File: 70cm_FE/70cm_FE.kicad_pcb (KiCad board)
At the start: 2 copper layers, 50 x 70 mm, 181 parts, among them J2 U.FL, J3 U.FL, J4 U.FL, Q1 2SC3356, Q2 2SC3356, Q3 2SC3356, Q4 2SC3356, U1 HT7533-1, U2 74HC14, U3 74HC14, U4 LM393, U5 M68710L

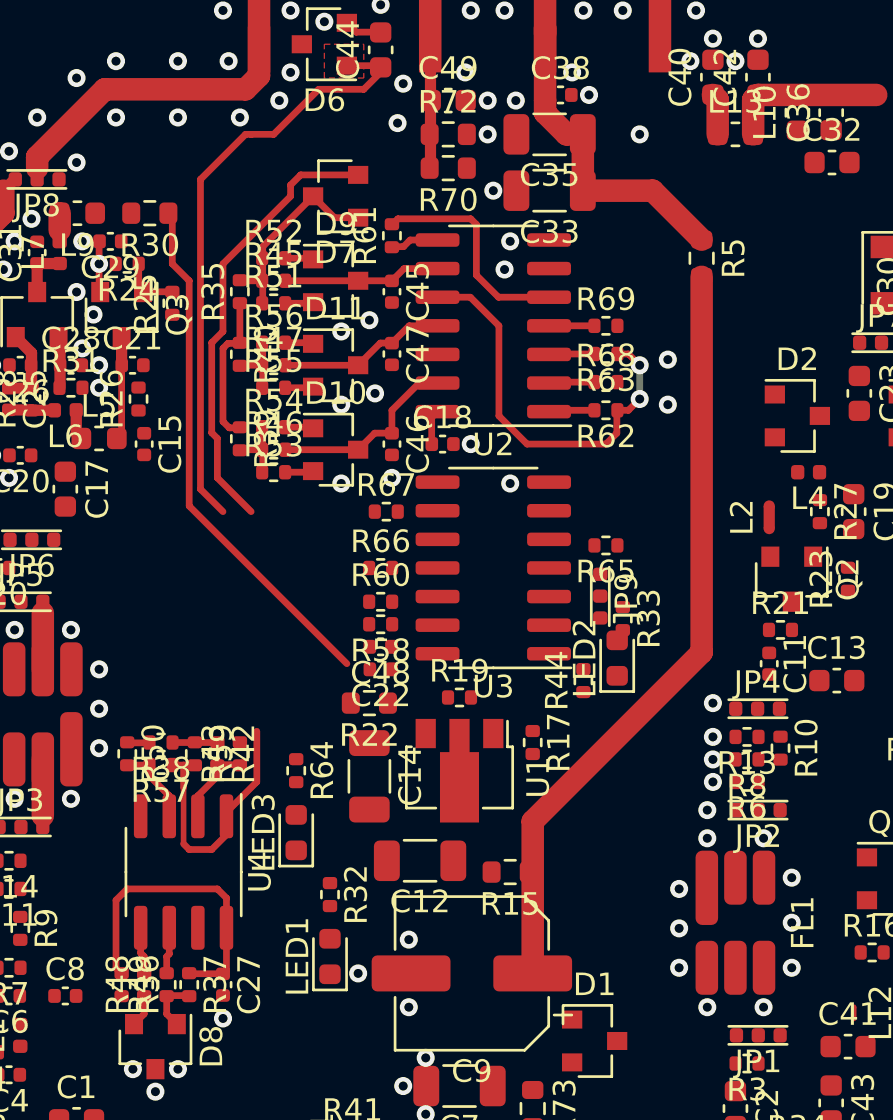
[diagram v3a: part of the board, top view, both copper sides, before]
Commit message: Change the order of inverters for better layout
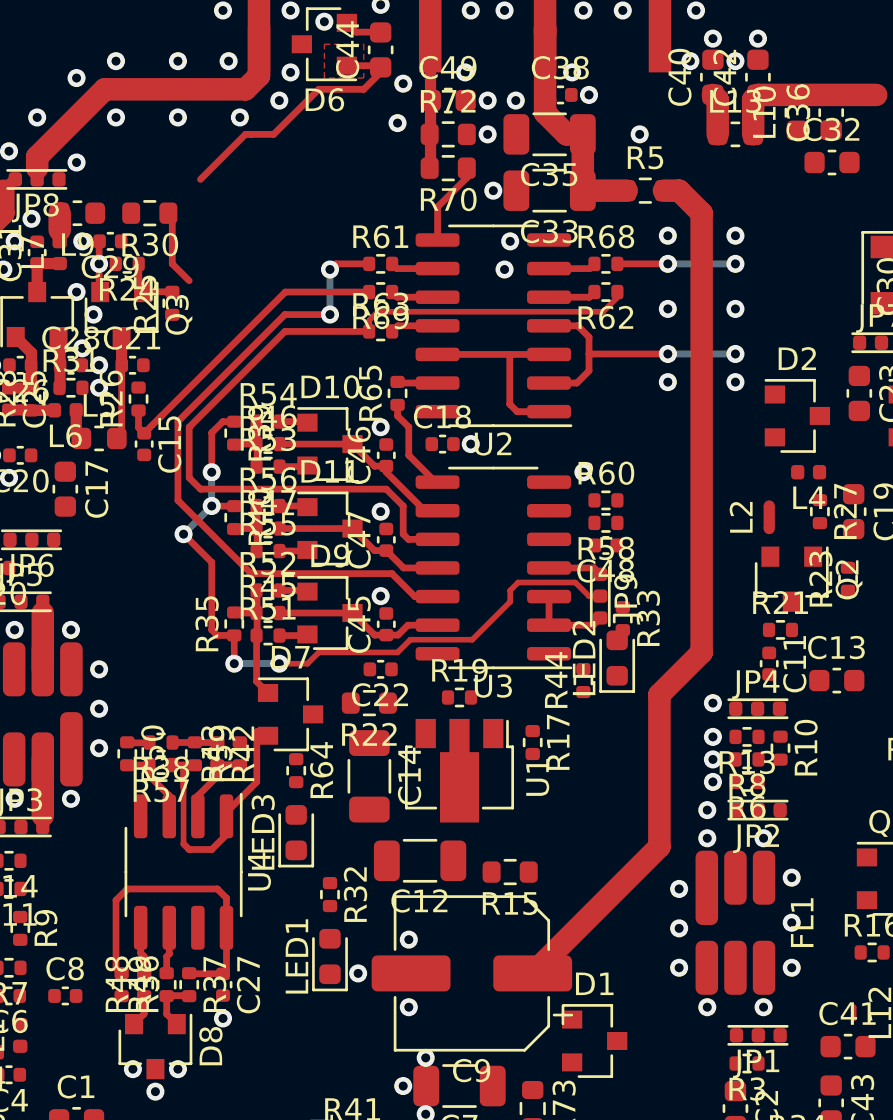
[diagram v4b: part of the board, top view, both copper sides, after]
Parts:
- removed R66, R67: 1k, Resistor_SMD:R_0402_1005Metric
- R65: value 1k -> 0
- moved D7 23.1 mm to (117.5, 92.5), turned to 0 degrees
- moved C45 14.8 mm to (121.8, 88.5), turned to 90 degrees
- moved D9 14.8 mm to (119.2, 88.0)
- moved R35 14.8 mm to (115.0, 88.5)
- moved R45 14.8 mm to (116.5, 88.0)
- moved R51 14.8 mm to (116.5, 89.0)
- moved R52 14.8 mm to (116.5, 87.0)
- moved R65 11.5 mm to (122.2, 78.2), turned to 90 degrees
- moved C48 11.0 mm to (131.5, 85.0)
- moved R58 11.0 mm to (131.5, 84.0)
- moved R60 11.0 mm to (131.5, 83.0)
- moved R69 10.1 mm to (121.5, 73.8), turned to 180 degrees
- moved R63 10.0 mm to (121.5, 75.5), turned to 0 degrees
- moved C47 8.25 mm to (121.8, 84.8), turned to 90 degrees
- moved D11 7.25 mm to (119.2, 84.2)
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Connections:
- D6 pad 3: Net-(D6-Pad3) -> (no net)
- R65 pad 1: GND -> /LNA_SEQ_OUT
- R65 pad 2: Net-(R65-Pad2) -> /LNA_EN_
- U2 pad 1: /~PIN_EN_~ -> /~LNA_EN_~
- U2 pad 10: /~PIN_SEQ_OUT~ -> /DRV_EN1
- U2 pad 11: /PIN_SEQ_IN -> /~DRV_EN_~
- U2 pad 12: /LNA_EN -> /~LNA_EN_~
- U2 pad 13: /~LNA_SEQ_IN~ -> /LNA_EN_
- U2 pad 2: /PIN_EN -> /LNA_EN
- U2 pad 3: /~DRV_EN_~ -> /~LNA_EN_~
- U2 pad 4: /DRV_EN1 -> /LNA_EN
- U2 pad 5: /~PA_EN_~ -> /~PIN_EN_~
- U2 pad 6: /PA_EN -> /PIN_EN
- U2 pad 8: /~PA_SEQ_OUT~ -> /PA_EN
- U2 pad 9: /PA_SEQ_IN -> /~PA_EN_~
- U3 pad 10: Net-(U3-Pad10) -> /~PIN_SEQ_OUT~
- U3 pad 11: Net-(R66-Pad2) -> /PIN_SEQ_IN
- U3 pad 12: /DET_OUT_ -> /~PA_SEQ_OUT~
- U3 pad 13: /DET_timing -> /PA_SEQ_IN
- U3 pad 5: Net-(R65-Pad2) -> /DET_timing
- U3 pad 6: Net-(U3-Pad6) -> /DET_OUT_
- U3 pad 8: Net-(U3-Pad8) -> /LNA_SEQ_OUT
- U3 pad 9: Net-(R67-Pad2) -> /~LNA_SEQ_IN~
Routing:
- net /~PA_SEQ_OUT~: track 2.15 -> 29.4 mm, vias 0 -> 2
- net /TX_ON: track 6.77 -> 32.6 mm, vias 0 -> 5
- net /VDD: track 40.5 -> 19.0 mm
- net /~OverTemp~: track 31.9 -> 12.0 mm
- net /~PIN_SEQ_OUT~: track 18.2 -> 36.8 mm, vias 2 -> 0
- net /TempSensor: track 27.7 -> 12.5 mm
- net /DRV_EN: track 0.00 -> 13.7 mm
- net /LNA_EN: track 0.00 -> 12.0 mm, vias 0 -> 2
- net /~LNA_EN_~: track 0.00 -> 9.04 mm
- net /~PA_EN_~: track 9.84 -> 2.10 mm
- net /PIN_bias: track 0.00 -> 5.24 mm, vias 0 -> 2
- net /V_in: track 34.0 -> 38.9 mm
- net /PA_VDD: track 14.8 -> 10.6 mm
- net /LNA_SEQ_OUT: track 0.00 -> 4.22 mm
- net /PA_EN: track 0.00 -> 3.73 mm
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
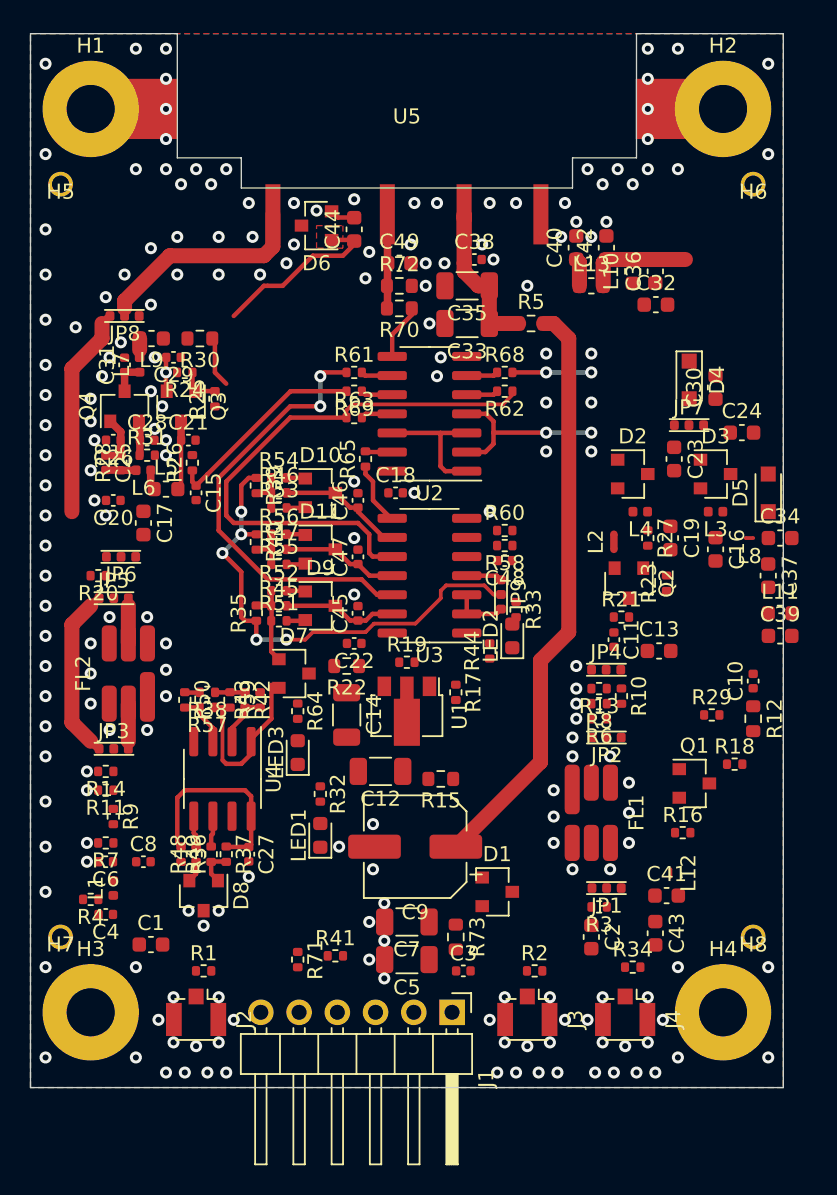
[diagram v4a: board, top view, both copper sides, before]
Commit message: Route a few traces
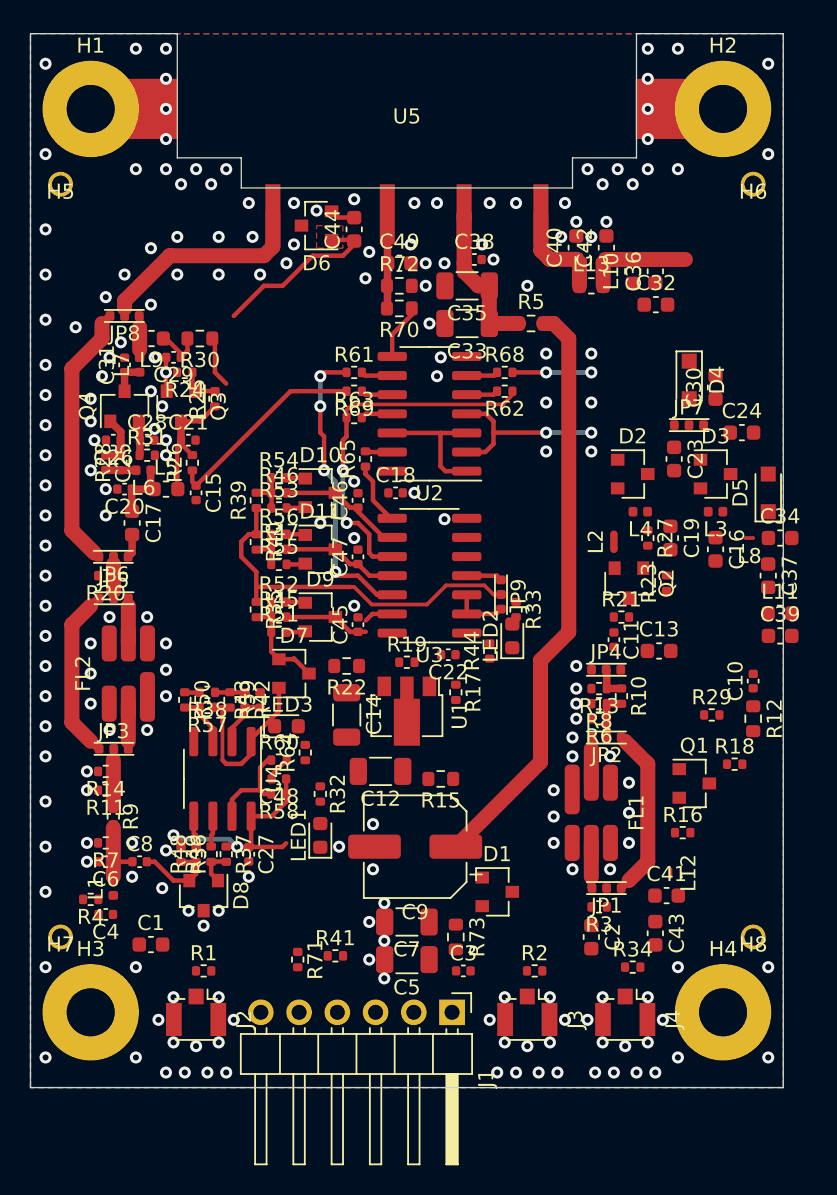
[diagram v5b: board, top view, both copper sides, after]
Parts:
- moved R58 22.3 mm to (116.5, 100.5)
- moved R60 21.4 mm to (116.5, 98.2)
- moved C48 20.9 mm to (116.5, 99.5)
- moved C22 6.29 mm to (127.8, 91.2)
- moved R64 2.80 mm to (118.2, 97.8), turned to 90 degrees
- moved LED3 1.90 mm to (117.0, 96.0), turned to 0 degrees
- moved C20 1.06 mm to (106.2, 80.2)
- moved R39 0.98 mm to (115.0, 81.0), turned to 90 degrees
- moved C17 0.75 mm to (106.8, 82.5)
- moved C45 0.75 mm to (121.8, 89.2)
- moved D9 0.75 mm to (119.2, 88.8)
- moved R45 0.75 mm to (116.5, 88.8)
- moved R51 0.75 mm to (116.5, 89.8)
- moved R52 0.75 mm to (116.5, 87.8)
- moved JP6 0.50 mm to (106.0, 84.8)
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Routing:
- net /~PIN_SEQ_OUT~: track 36.8 -> 23.8 mm, vias 0 -> 2
- net /RXSAW_bypass: track 0.00 -> 11.1 mm
- net /~PA_SEQ_OUT~: track 29.4 -> 19.7 mm, vias 2 -> 4
- net /TX_ON: track 32.6 -> 24.9 mm, vias 5 -> 0
- net /DET_COMPout: track 0.00 -> 6.52 mm
- net /PA_out: track 1.84 -> 6.83 mm
- net Net-(C6-Pad1): track 0.00 -> 4.54 mm
- net /DET_RF: track 1.47 -> 5.81 mm
- net /DRV_bias: track 4.59 -> 8.34 mm
- net Net-(JP3-Pad2): track 0.00 -> 3.72 mm
- net /DRV_bypass: track 14.1 -> 17.4 mm
- net Net-(C29-Pad1): track 0.00 -> 3.27 mm
- net Net-(JP2-Pad2): track 0.00 -> 3.23 mm
- net /VDD: track 19.0 -> 22.2 mm, vias 0 -> 2
- net /RXSAW_OUT: track 0.00 -> 3.02 mm
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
